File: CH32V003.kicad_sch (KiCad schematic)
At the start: 10 parts, among them J7 Program, SW1 SW_SPST, U5 CH32V003F4U6, X1 X322525MOB4SI

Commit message: commit before removing all the diodes :"
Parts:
- J7: KiLib_Generator (none) -> connector/pin_header_socket
- R12, R13: Field4 (none) -> ${REFERENCE}
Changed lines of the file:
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@@
+			)
+		)
+		(property "Field4" "${REFERENCE}"
+			(at 250.19 59.69 0)
+			(hide yes)
+			(show_name no)
+			(do_not_autoplace no)
+			(effects
+				(font
+					(size 1.27 1.27)
+				)
 			)
 		)
@@
 			)
 		)
+		(property "KiLib_Generator" "connector/pin_header_socket"
+			(at 69.85 142.24 0)
+			(hide yes)
+			(show_name no)
+			(do_not_autoplace no)
+			(effects
+				(font
+					(size 1.27 1.27)
+				)
+			)
+		)
 		(pin "3"
 		)
@@
 			(at 134.62 140.97 0)
 			(hide yes)
+			(show_name no)
+			(do_not_autoplace no)
+			(effects
+				(font
+					(size 1.27 1.27)
+				)
+			)
+		)
+		(property "Field4" "${REFERENCE}"
+			(at 134.62 140.97 0)
+			(hide yes)

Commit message: finished routing
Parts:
- removed C7, C8: C, symbol Device:C
- removed SW1: SW_SPST, symbol Switch:SW_SPST
- removed U5: CH32V003F4U6, PCM_JLCPCB:QFN-20-1EP_3x3mm_P0.4mm_EP1.65x1.65mm, symbol PCM_JLCPCB-Extended:MCU, CH32V003F4U6
- removed X1: X322525MOB4SI, PCM_JLCPCB:OSC-SMD_4P-L3.2-W2.5-BL, symbol PCM_JLCPCB-Crystals:Crystal, 25MHz, 11pF
- added C3, C5: 12pF, PCM_JLCPCB:C_0603, symbol PCM_JLCPCB-Capacitors:0603,12pF
- added S1: Tactile Button, 160gf, PCM_JLCPCB:SW_TS-1088-AR02016, symbol PCM_JLCPCB-Connectors_Buttons:Tactile Button, 160gf, 12V, 50mA, 4.0mm
- added U5: CH32V003FxPx, PCM_JLCPCB:TSSOP-20_4.4x6.5mm_P0.65mm, symbol MCU_WCH_RiscV:CH32V003FxPx
- added X2: X322525MOB4SI, PCM_JLCPCB:OSC-SMD_4P-L3.2-W2.5-BL, symbol PCM_JLCPCB-Crystals:Crystal, 25MHz, 11pF
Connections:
- net +3V3: now also U5.9 (VDD)
- net GND: now also C3.2, C5.2, S1.2 (B), U5.7 (VSS), X2.2 (GND), X2.4 (GND)
- net OSCI: now also C5.1, U5.5 (PA1), X2.3 (OSC)
- net OSCO: now also C3.1, U5.6 (PA2), X2.1 (OSC)
- net PC0: now also U5.10 (PC0)
- net PC1 (SDA): now also U5.11 (PC1)
- net PC2 (SCL): now also U5.12 (PC2)
- net PC3: now also U5.13 (PC3)
- net PC4: now also U5.14 (PC4)
- net PC5 (SCK): now also U5.15 (PC5)
- net PC6 (MOSI): now also U5.16 (PC6)
- net PC7 (MISO): now also U5.17 (PC7)
- net PD0: now also U5.8 (PD0)
- net PD2: now also U5.19 (PD2)
- net PD3: now also U5.20 (PD3)
- net PD4: now also U5.1 (PD4)
- net PD5 (TX): now also U5.2 (PD5)
- net PD6 (RX): now also U5.3 (PD6)
- net PD7 (NRST): now also S1.1 (A), U5.4 (PD7)
- net SWIO: now also U5.18 (PD1)
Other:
- moved on the sheet: R12

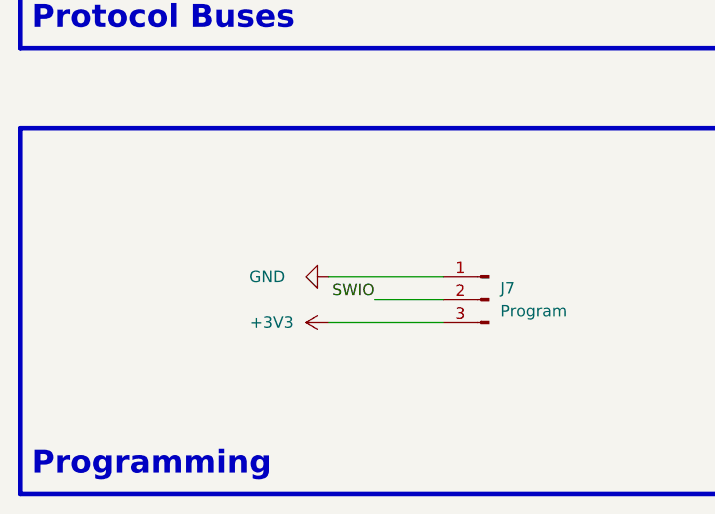
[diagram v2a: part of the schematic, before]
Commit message: BREAKING: updated CH32v003 programming pinout
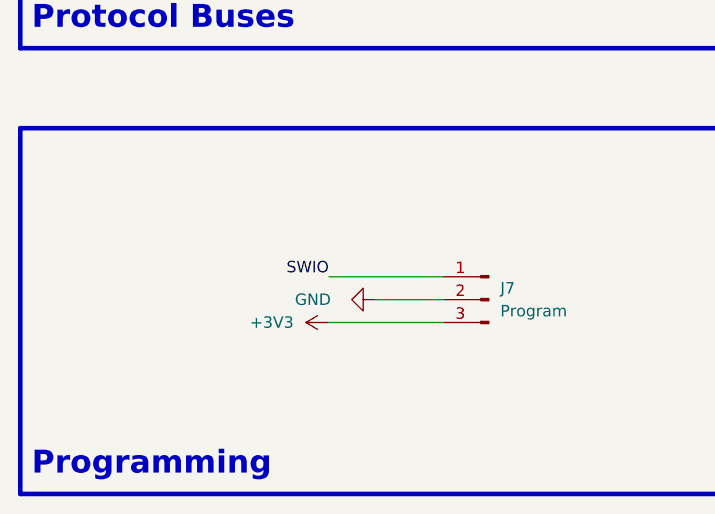
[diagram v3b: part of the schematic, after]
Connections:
- net GND: now also J7.2 (Pin_2); no longer J7.1 (Pin_1)
- net SWIO: now also J7.1 (Pin_1); no longer J7.2 (Pin_2)
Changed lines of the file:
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@@
 	(title_block
 		(title "MMS3_hat_ruski_wentylator_do_pieca")
-		(rev "A")
+		(rev "1.1")
 		(company "MiniModucard System")
 		(comment 1 "Wojciech Szafrański")
@@
 	)
 	(label "SWIO"
-		(at 57.15 142.24 180)
+		(at 52.07 139.7 180)
 		(effects
 			(font
@@
 	(symbol
 		(lib_id "power:GND")
-		(at 52.07 139.7 270)
+		(at 57.15 142.24 270)
 		(unit 1)
 		(body_style 1)
@@
 		(dnp no)
 		(property "Reference" "#PWR055"
-			(at 45.72 139.7 0)
+			(at 50.8 142.24 0)
 			(hide yes)
 			(show_name no)
@@
 		)
 		(property "Value" "GND"
-			(at 45.212 139.7 90)
+			(at 50.292 142.24 90)
 			(show_name no)
 			(do_not_autoplace no)
@@
 		)
 		(property "Footprint" ""
-			(at 52.07 139.7 0)
+			(at 57.15 142.24 0)
 			(hide yes)
 			(show_name no)
@@
 		)
 		(property "Datasheet" ""
-			(at 52.07 139.7 0)
+			(at 57.15 142.24 0)
 			(hide yes)
 			(show_name no)
@@
 		)
 		(property "Description" "Power symbol creates a global label with name \"GND\" , ground"
-			(at 52.07 139.7 0)
-			(hide yes)
-			(show_name no)
+			(at 57.15 142.24 0)
+			(hide yes)
+			(show_name no)
